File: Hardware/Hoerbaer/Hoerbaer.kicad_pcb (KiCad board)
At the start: 4 copper layers, 186 parts, among them J1 I2C, J10 LEDS, J11 LEDS, J12 Battery 1S Li-Ion, J13 JTAG, J14 Speaker_L, J15 Speaker_R, J16 USB2_UART, J2 DISPLAY, J3 Micro_SD_Card_Det1, J4 USB1, J5 ENCODER, J6 BUTTONS, J7 BUTTONS, J8 BUTTONS, J9 LEDS, Q1 DMG3415UQ-7, Q5 S8050, Q6 S8050, SW1 RESET, SW2 PROG, U1 ESP32 S3 MINI, U10 TAS5805M, U11 CH343P, U12 MAX17048G, U13 TPS61288, U2 PCF8574TS, U3 PCF8574TS, U4 PCF8574TS, U5 TLC59108xPW, U6 TLC59108xPW, U7 TLC59108xPW, U8 MCP73831T-2ACI/OT (4.2V), U9 TPS63001

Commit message: More numbers, changed HBI input package, i2c addresses, layout.
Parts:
- added C63: 100nF, Capacitor_SMD:C_0402_1005Metric, F.Cu at (52.5, -14.6)
- added D4: GREEN, LED_SMD:LED_0603_1608Metric, F.Cu at (155.4, -106.4)
- added H1: MountingHole_Pad, MountingHole:MountingHole_3.2mm_M3_Pad_Via, F.Cu at (31.3, 132.5)
- added H2: MountingHole_Pad, MountingHole:MountingHole_3.2mm_M3_Pad_Via, F.Cu at (31.3, 140.4)
- added H3: MountingHole_Pad, MountingHole:MountingHole_3.2mm_M3_Pad_Via, F.Cu at (31.3, 148.4)
- added H4: MountingHole_Pad, MountingHole:MountingHole_3.2mm_M3_Pad_Via, F.Cu at (31.3, 156.3)
- added J17: RST_BOOT, Connector_PinHeader_2.54mm:PinHeader_1x03_P2.54mm_Vertical, F.Cu at (146.7, -99.4)
- added R56: 5.1kΩ, Resistor_SMD:R_0402_1005Metric, F.Cu at (154.8, -104.1)
- J12, J14, J15: footprint Connector_Wire:SolderWire-0.75sqmm_1x02_P7mm_D1.25mm_OD3.5mm -> Connector_Phoenix_MSTB:PhoenixContact_MSTBVA_2,5_2-G-5,08_1x02_P5.08mm_Vertical
- J5: footprint Connector_PinHeader_2.54mm:PinHeader_1x03_P2.54mm_Vertical -> Connector_PinHeader_2.54mm:PinHeader_1x04_P2.54mm_Vertical
- U2, U3, U4: value PCF8574TS -> PCF8574APWR; footprint Package_SO:SOIC-16W_7.5x10.3mm_P1.27mm -> Package_SO:SSOP-20_4.4x6.5mm_P0.65mm
- moved D3 284.3 mm to (61.9, -85.7)
- moved C62 276.7 mm to (54.2, -86.0), turned to 180 degrees
- moved Q1 275.4 mm to (60.1, -89.6)
- moved C12 274.0 mm to (49.7, -70.8)
- moved C15 272.8 mm to (56.8, -74.2), turned to -90 degrees
- moved R62 269.9 mm to (65.3, -146.1)
- moved L1 269.8 mm to (50.2, -77.1)
- moved TP6 269.3 mm to (44.0, -71.0)
- moved R48 268.7 mm to (57.0, -90.6), turned to 180 degrees
- moved U9 266.0 mm to (50.2, -73.4), turned to -90 degrees
- moved R61 263.1 mm to (67.4, -140.7)
- moved R46 262.2 mm to (45.0, -71.0)
- moved R63 261.2 mm to (84.7, -149.4), turned to 180 degrees
- moved U8 261.2 mm to (72.7, -78.5)
- moved C13 261.1 mm to (47.1, -74.0), turned to -90 degrees
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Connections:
- net Net-(C21-Pad1) renamed /Power/12V_SW
- net Net-(D3-K) renamed /Power/SWITCHER_VIN
- net Net-(U9-L1) renamed /Power/3V3_L1
- net Net-(U9-L2) renamed /Power/3V3_L2
- U1 pad 17: unconnected-(U1-IO13-Pad17) -> Net-(U1-IO13)
- U2 pad 1: GND -> /HBI_INT
- U2 pad 10: Net-(J6-Pin_12) -> Net-(J6-Pin_2)
- U2 pad 11: Net-(J6-Pin_14) -> Net-(J6-Pin_4)
- U2 pad 12: Net-(J6-Pin_16) -> Net-(J6-Pin_6)
- U2 pad 13: /HBI_INT -> unconnected-(U2-NC-Pad13)
- U2 pad 14: /I2C1_SCL -> Net-(J6-Pin_8)
- U2 pad 15: /I2C1_SDA -> GND
- U2 pad 16: VCC -> Net-(J6-Pin_10)
- U2 pad 2: GND -> /I2C1_SCL
- U2 pad 3: GND -> unconnected-(U2-NC-Pad3)
- U2 pad 4: Net-(J6-Pin_2) -> /I2C1_SDA
- U2 pad 5: Net-(J6-Pin_4) -> VCC
- U2 pad 6: Net-(J6-Pin_6) -> GND
- U2 pad 7: Net-(J6-Pin_8) -> GND
- U2 pad 8: GND -> unconnected-(U2-NC-Pad8)
- U2 pad 9: Net-(J6-Pin_10) -> GND
- U3 pad 1: VCC -> /HBI_INT
- U3 pad 10: Net-(J7-Pin_12) -> Net-(J7-Pin_2)
- U3 pad 11: Net-(J7-Pin_14) -> Net-(J7-Pin_4)
- U3 pad 12: Net-(J7-Pin_16) -> Net-(J7-Pin_6)
- U3 pad 13: /HBI_INT -> unconnected-(U3-NC-Pad13)
- U3 pad 14: /I2C1_SCL -> Net-(J7-Pin_8)
- U3 pad 15: /I2C1_SDA -> GND
- U3 pad 16: VCC -> Net-(J7-Pin_10)
- U3 pad 2: GND -> /I2C1_SCL
- U3 pad 3: GND -> unconnected-(U3-NC-Pad3)
- U3 pad 4: Net-(J7-Pin_2) -> /I2C1_SDA
- U3 pad 5: Net-(J7-Pin_4) -> VCC
- U3 pad 6: Net-(J7-Pin_6) -> VCC
- U3 pad 7: Net-(J7-Pin_8) -> GND
- U3 pad 8: GND -> unconnected-(U3-NC-Pad8)
- U3 pad 9: Net-(J7-Pin_10) -> GND
- U4 pad 1: GND -> /HBI_INT
- U4 pad 10: Net-(J8-Pin_12) -> Net-(J8-Pin_2)
- U4 pad 11: Net-(J8-Pin_14) -> Net-(J8-Pin_4)
- U4 pad 12: Net-(J8-Pin_16) -> Net-(J8-Pin_6)
- U4 pad 13: /HBI_INT -> unconnected-(U4-NC-Pad13)
- U4 pad 14: /I2C1_SCL -> Net-(J8-Pin_8)
- U4 pad 15: /I2C1_SDA -> GND
- U4 pad 16: VCC -> Net-(J8-Pin_10)
- U4 pad 2: VCC -> /I2C1_SCL
- U4 pad 3: GND -> unconnected-(U4-NC-Pad3)
- U4 pad 4: Net-(J8-Pin_2) -> /I2C1_SDA
- U4 pad 5: Net-(J8-Pin_4) -> VCC
- U4 pad 6: Net-(J8-Pin_6) -> GND
- U4 pad 7: Net-(J8-Pin_8) -> VCC
- U4 pad 8: GND -> unconnected-(U4-NC-Pad8)
- U4 pad 9: Net-(J8-Pin_10) -> GND
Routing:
- net Net-(J16-CC1): track 0.00 -> 1.86 mm
- added copper zone on F.Cu, net +12V
- added copper zone on F.Cu, net /Power/12V_SW
- added copper zone on F.Cu, net /Power/3V3_L1
- added copper zone on F.Cu, net /Power/3V3_L2
- added copper zone on F.Cu, net /Power/SWITCHER_VIN
- added copper zone on F.Cu, net GNDPWR
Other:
- board outline added: 180 x 89 mm

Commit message: Layout drc error free
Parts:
- removed H4: MountingHole_Pad, MountingHole:MountingHole_3.2mm_M3_Pad_Via
- removed J10, J11: LEDS, Connector_PinHeader_2.54mm:PinHeader_2x08_P2.54mm_Vertical
- added C64: 100nF, Capacitor_SMD:C_0402_1005Metric, F.Cu at (117.2, 69.3)
- added C65: 10µF, Capacitor_SMD:C_0805_2012Metric, F.Cu at (66.2, 106.7)
- C56, C57: value 100nF -> 1uF
- C60: value 1nF -> 4.7nF
- C61: value 30pF -> 27pF
- J1: footprint Connector_PinHeader_2.54mm:PinHeader_1x03_P2.54mm_Vertical -> Connector_PinHeader_2.54mm:PinHeader_1x04_P2.54mm_Vertical
- J6: value BUTTONS -> PAW_A; footprint Connector_PinHeader_2.54mm:PinHeader_2x08_P2.54mm_Vertical -> Connector_PinHeader_2.54mm:PinHeader_2x12_P2.54mm_Vertical
- J7: value BUTTONS -> PAW_B; footprint Connector_PinHeader_2.54mm:PinHeader_2x08_P2.54mm_Vertical -> Connector_PinHeader_2.54mm:PinHeader_2x12_P2.54mm_Vertical
- J8: value BUTTONS -> PAW_C; footprint Connector_PinHeader_2.54mm:PinHeader_2x08_P2.54mm_Vertical -> Connector_PinHeader_2.54mm:PinHeader_2x12_P2.54mm_Vertical
- J9: value LEDS -> PAW_D; footprint Connector_PinHeader_2.54mm:PinHeader_2x08_P2.54mm_Vertical -> Connector_PinHeader_2.54mm:PinHeader_2x12_P2.54mm_Vertical
- R55: value 36.6kΩ -> 47kΩ
- TP1, TP10, TP2, TP3, TP4, TP5, TP6, TP7, TP8, TP9: moved to F.Cu
- moved J14 295.1 mm to (116.5, 142.5), turned to 180 degrees
- moved R63 287.9 mm to (115.0, 136.9), turned to 90 degrees
- moved C51 286.7 mm to (113.5, 137.4), turned to 0 degrees
- moved C46 285.8 mm to (113.5, 136.4), turned to 0 degrees
- moved R64 284.5 mm to (110.8, 136.9), turned to 90 degrees
- moved C52 283.3 mm to (109.3, 137.4), turned to 0 degrees
- moved FB2 282.4 mm to (112.3, 133.5), turned to -90 degrees
- moved C47 282.4 mm to (109.3, 136.4), turned to 0 degrees
- moved C54 281.5 mm to (104.9, 137.4), turned to 180 degrees
- moved J15 280.9 mm to (98.0, 143.5), turned to 0 degrees
- moved C45 280.4 mm to (114.8, 126.5), turned to 0 degrees
- moved FB3 279.5 mm to (108.8, 133.5), turned to -90 degrees
- moved R66 279.3 mm to (103.4, 136.9), turned to 90 degrees
- moved C43 279.2 mm to (112.0, 128.8), turned to 0 degrees
- moved C49 279.0 mm to (104.9, 136.4), turned to 180 degrees
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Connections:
- net Net-(J14-Pin_1) renamed /Audio/SPEAKER_A+
- net Net-(J14-Pin_2) renamed /Audio/SPEAKER_A-
- net Net-(J15-Pin_1) renamed /Audio/SPEAKER_B+
- net Net-(J15-Pin_2) renamed /Audio/SPEAKER_B-
- net Net-(U10-OUT_A+) renamed /Audio/AMP_OUT_A+
- net Net-(U10-OUT_A-) renamed /Audio/AMP_OUT_A-
- net Net-(U10-OUT_B+) renamed /Audio/AMP_OUT_B+
- net Net-(U10-OUT_B-) renamed /Audio/AMP_OUT_B-
- C25 pad 2: GNDPWR -> GND
- C56 pad 1: Net-(U11-VIO) -> VCC
- C57 pad 1: Net-(U11-VDD5) -> /USB_UART/USB2_VBUS
- J3 pad 11: unconnected-(J3-SHIELD-Pad11) -> GND
- J6 pad 1: Net-(J6-Pin_1) -> /HBI/PAW_A_B1
- J6 pad 10: Net-(J6-Pin_10) -> GND
- J6 pad 11: Net-(J6-Pin_1) -> /HBI/PAW_A_D3
- J6 pad 12: Net-(J6-Pin_12) -> +12V
- J6 pad 13: Net-(J6-Pin_1) -> /HBI/PAW_A_B4
- J6 pad 14: Net-(J6-Pin_14) -> GND
- J6 pad 15: GND -> /HBI/PAW_A_D4
- J6 pad 16: Net-(J6-Pin_16) -> +12V
- J6 pad 2: Net-(J6-Pin_2) -> GND
- J6 pad 3: Net-(J6-Pin_1) -> /HBI/PAW_A_D1
- J6 pad 4: Net-(J6-Pin_4) -> +12V
- J6 pad 5: Net-(J6-Pin_1) -> /HBI/PAW_A_B2
- J6 pad 6: Net-(J6-Pin_6) -> GND
- J6 pad 7: Net-(J6-Pin_1) -> /HBI/PAW_A_D2
- J6 pad 8: Net-(J6-Pin_8) -> +12V
- J6 pad 9: Net-(J6-Pin_1) -> /HBI/PAW_A_B3
- J7 pad 1: Net-(J7-Pin_1) -> /HBI/PAW_B_B1
- J7 pad 10: Net-(J7-Pin_10) -> GND
- J7 pad 11: Net-(J7-Pin_1) -> /HBI/PAW_B_D3
- J7 pad 12: Net-(J7-Pin_12) -> +12V
- J7 pad 13: Net-(J7-Pin_1) -> /HBI/PAW_B_B4
- J7 pad 14: Net-(J7-Pin_14) -> GND
- J7 pad 15: GND -> /HBI/PAW_B_D4
- J7 pad 16: Net-(J7-Pin_16) -> +12V
- J7 pad 2: Net-(J7-Pin_2) -> GND
- J7 pad 3: Net-(J7-Pin_1) -> /HBI/PAW_B_D1
- J7 pad 4: Net-(J7-Pin_4) -> +12V
- J7 pad 5: Net-(J7-Pin_1) -> /HBI/PAW_B_B2
- J7 pad 6: Net-(J7-Pin_6) -> GND
- J7 pad 7: Net-(J7-Pin_1) -> /HBI/PAW_B_D2
- J7 pad 8: Net-(J7-Pin_8) -> +12V
- J7 pad 9: Net-(J7-Pin_1) -> /HBI/PAW_B_B3
- J8 pad 1: Net-(J8-Pin_1) -> /HBI/PAW_C_B1
- J8 pad 10: Net-(J8-Pin_10) -> GND
- J8 pad 11: Net-(J8-Pin_1) -> /HBI/PAW_C_D3
- J8 pad 12: Net-(J8-Pin_12) -> +12V
- J8 pad 13: Net-(J8-Pin_1) -> /HBI/PAW_C_B4
- J8 pad 14: Net-(J8-Pin_14) -> GND
- J8 pad 15: GND -> /HBI/PAW_C_D4
- J8 pad 16: Net-(J8-Pin_16) -> +12V
- J8 pad 2: Net-(J8-Pin_2) -> GND
- J8 pad 3: Net-(J8-Pin_1) -> /HBI/PAW_C_D1
- J8 pad 4: Net-(J8-Pin_4) -> +12V
- J8 pad 5: Net-(J8-Pin_1) -> /HBI/PAW_C_B2
- J8 pad 6: Net-(J8-Pin_6) -> GND
- J8 pad 7: Net-(J8-Pin_1) -> /HBI/PAW_C_D2
- J8 pad 8: Net-(J8-Pin_8) -> +12V
- J8 pad 9: Net-(J8-Pin_1) -> /HBI/PAW_C_B3
- J9 pad 1: +12V -> /HBI/PAW_D_B1
- J9 pad 10: Net-(J9-Pin_10) -> GND
- J9 pad 11: +12V -> /HBI/PAW_D_D3
- J9 pad 12: Net-(J9-Pin_12) -> +12V
- J9 pad 13: +12V -> /HBI/PAW_D_B4
- J9 pad 14: Net-(J9-Pin_14) -> GND
- J9 pad 15: +12V -> /HBI/PAW_D_D4
- J9 pad 16: Net-(J9-Pin_16) -> +12V
- J9 pad 2: Net-(J9-Pin_2) -> GND
- J9 pad 3: +12V -> /HBI/PAW_D_D1
- J9 pad 4: Net-(J9-Pin_4) -> +12V
- J9 pad 5: +12V -> /HBI/PAW_D_B2
- J9 pad 6: Net-(J9-Pin_6) -> GND
- J9 pad 7: +12V -> /HBI/PAW_D_D2
- J9 pad 8: Net-(J9-Pin_8) -> +12V
- J9 pad 9: +12V -> /HBI/PAW_D_B3
- R19 pad 2: Net-(J6-Pin_2) -> /HBI/PAW_A_B1
- R20 pad 2: Net-(J7-Pin_2) -> /HBI/PAW_B_B3
- R21 pad 2: Net-(J8-Pin_2) -> /HBI/PAW_C_B5
- R22 pad 2: Net-(J6-Pin_4) -> /HBI/PAW_A_B2
- R23 pad 2: Net-(J7-Pin_4) -> /HBI/PAW_B_B4
- R24 pad 2: Net-(J8-Pin_4) -> /HBI/PAW_C_B6
- R25 pad 2: Net-(J6-Pin_6) -> /HBI/PAW_A_B3
- R26 pad 2: Net-(J7-Pin_6) -> /HBI/PAW_B_B5
- R27 pad 2: Net-(J8-Pin_6) -> /HBI/PAW_D_B1
- R28 pad 2: Net-(J6-Pin_8) -> /HBI/PAW_A_B4
- R29 pad 2: Net-(J7-Pin_8) -> /HBI/PAW_B_B6
- R30 pad 2: Net-(J8-Pin_8) -> /HBI/PAW_D_B2
- R31 pad 2: Net-(J6-Pin_10) -> /HBI/PAW_A_B5
- R32 pad 2: Net-(J7-Pin_10) -> /HBI/PAW_C_B1
- R33 pad 2: Net-(J8-Pin_10) -> /HBI/PAW_D_B3
- R34 pad 2: Net-(J6-Pin_12) -> /HBI/PAW_A_B6
- R35 pad 2: Net-(J7-Pin_12) -> /HBI/PAW_C_B2
- R36 pad 2: Net-(J8-Pin_12) -> /HBI/PAW_D_B4
- R37 pad 2: Net-(J6-Pin_14) -> /HBI/PAW_B_B1
- R38 pad 2: Net-(J7-Pin_14) -> /HBI/PAW_C_B3
- R39 pad 2: Net-(J8-Pin_14) -> /HBI/PAW_D_B5
- R40 pad 2: Net-(J6-Pin_16) -> /HBI/PAW_B_B2
- R41 pad 2: Net-(J7-Pin_16) -> /HBI/PAW_C_B4
- R42 pad 2: Net-(J8-Pin_16) -> /HBI/PAW_D_B6
- U11 pad 1: Net-(U11-VIO) -> VCC
- U11 pad 3: Net-(U11-VDD5) -> /USB_UART/USB2_VBUS
- U2 pad 10: Net-(J6-Pin_2) -> /HBI/PAW_A_B1
- U2 pad 11: Net-(J6-Pin_4) -> /HBI/PAW_A_B2
- U2 pad 12: Net-(J6-Pin_6) -> /HBI/PAW_A_B3
- U2 pad 14: Net-(J6-Pin_8) -> /HBI/PAW_A_B4
- U2 pad 16: Net-(J6-Pin_10) -> /HBI/PAW_A_B5
- U2 pad 17: Net-(J6-Pin_12) -> /HBI/PAW_A_B6
- U2 pad 19: Net-(J6-Pin_14) -> /HBI/PAW_B_B1
- U2 pad 20: Net-(J6-Pin_16) -> /HBI/PAW_B_B2
- U3 pad 10: Net-(J7-Pin_2) -> /HBI/PAW_B_B3
- U3 pad 11: Net-(J7-Pin_4) -> /HBI/PAW_B_B4
- U3 pad 12: Net-(J7-Pin_6) -> /HBI/PAW_B_B5
- U3 pad 14: Net-(J7-Pin_8) -> /HBI/PAW_B_B6
- U3 pad 16: Net-(J7-Pin_10) -> /HBI/PAW_C_B1
- U3 pad 17: Net-(J7-Pin_12) -> /HBI/PAW_C_B2
- U3 pad 19: Net-(J7-Pin_14) -> /HBI/PAW_C_B3
- U3 pad 20: Net-(J7-Pin_16) -> /HBI/PAW_C_B4
- U4 pad 10: Net-(J8-Pin_2) -> /HBI/PAW_C_B5
- U4 pad 11: Net-(J8-Pin_4) -> /HBI/PAW_C_B6
- U4 pad 12: Net-(J8-Pin_6) -> /HBI/PAW_D_B1
- U4 pad 14: Net-(J8-Pin_8) -> /HBI/PAW_D_B2
- U4 pad 16: Net-(J8-Pin_10) -> /HBI/PAW_D_B3
- U4 pad 17: Net-(J8-Pin_12) -> /HBI/PAW_D_B4
- U4 pad 19: Net-(J8-Pin_14) -> /HBI/PAW_D_B5
- U4 pad 20: Net-(J8-Pin_16) -> /HBI/PAW_D_B6
- U5 pad 10: Net-(J9-Pin_8) -> /HBI/PAW_A_D4
- U5 pad 11: Net-(J9-Pin_10) -> /HBI/PAW_A_D5
- U5 pad 12: Net-(J9-Pin_12) -> /HBI/PAW_A_D6
- U5 pad 14: Net-(J9-Pin_14) -> /HBI/PAW_B_D1
- U5 pad 15: Net-(J9-Pin_16) -> /HBI/PAW_B_D2
- U5 pad 6: Net-(J9-Pin_2) -> /HBI/PAW_A_D1
- U5 pad 7: Net-(J9-Pin_4) -> /HBI/PAW_A_D2
- U5 pad 9: Net-(J9-Pin_6) -> /HBI/PAW_A_D3
- U6 pad 10: Net-(J10-Pin_8) -> /HBI/PAW_B_D6
- U6 pad 11: Net-(J10-Pin_10) -> /HBI/PAW_C_D1
- U6 pad 12: Net-(J10-Pin_12) -> /HBI/PAW_C_D2
- U6 pad 14: Net-(J10-Pin_14) -> /HBI/PAW_C_D3
- U6 pad 15: Net-(J10-Pin_16) -> /HBI/PAW_C_D4
- U6 pad 6: Net-(J10-Pin_2) -> /HBI/PAW_B_D3
- U6 pad 7: Net-(J10-Pin_4) -> /HBI/PAW_B_D4
- U6 pad 9: Net-(J10-Pin_6) -> /HBI/PAW_B_D5
- U7 pad 10: Net-(J11-Pin_8) -> /HBI/PAW_D_D2
- U7 pad 11: Net-(J11-Pin_10) -> /HBI/PAW_D_D3
- U7 pad 12: Net-(J11-Pin_12) -> /HBI/PAW_D_D4
- U7 pad 14: Net-(J11-Pin_14) -> /HBI/PAW_D_D5
- U7 pad 15: Net-(J11-Pin_16) -> /HBI/PAW_D_D6
- U7 pad 6: Net-(J11-Pin_2) -> /HBI/PAW_C_D5
- U7 pad 7: Net-(J11-Pin_4) -> /HBI/PAW_C_D6
- U7 pad 9: Net-(J11-Pin_6) -> /HBI/PAW_D_D1
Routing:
- net /I2C1_SCL: track 0.00 -> 203.1 mm, vias 0 -> 10
- net /I2C1_SDA: track 0.00 -> 201.6 mm, vias 0 -> 9
- net GND: track 0.00 -> 165.5 mm, vias 0 -> 176
- net /HBI_INT: track 0.00 -> 116.5 mm, vias 0 -> 5
- net /HBI_RST: track 0.00 -> 111.5 mm, vias 0 -> 6
- net +12V: track 0.00 -> 95.6 mm, vias 0 -> 28
- net /MCU_~{RST}: track 0.00 -> 85.8 mm, vias 0 -> 6
- net /MCU_IO0: track 0.00 -> 80.2 mm, vias 0 -> 2
- net VCC: track 0.00 -> 80.2 mm, vias 0 -> 58
- net /CODEC_~{PDN}: track 0.00 -> 73.6 mm, vias 0 -> 2
- net /I2S1_DOUT: track 0.00 -> 69.5 mm, vias 0 -> 2
- net /I2S1_BCLK: track 0.00 -> 69.1 mm, vias 0 -> 2
- net /I2S1_WS: track 0.00 -> 69.0 mm, vias 0 -> 2
- net /MCU_TXD: track 0.00 -> 63.7 mm, vias 0 -> 2
- net /MCU_RXD: track 0.00 -> 62.8 mm, vias 0 -> 2
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- added copper zone on In1.Cu, net +12V
- added copper zone on F.Cu, net +BATT
- added copper zone on F.Cu, net /Audio/AMP_OUT_A+
- added copper zone on F.Cu, net /Audio/AMP_OUT_A-
- added copper zone on F.Cu, net /Audio/AMP_OUT_B+
- added copper zone on F.Cu, net /Audio/AMP_OUT_B-
- added copper zone on F.Cu, net /Audio/PVDD
- added copper zone on In1.Cu, net /Audio/PVDD
- added copper zone on F.Cu, net /Audio/SPEAKER_A+
- added copper zone on F.Cu, net /Audio/SPEAKER_A-
- added copper zone on F.Cu, net /Audio/SPEAKER_B+
- added copper zone on F.Cu, net /Audio/SPEAKER_B-
- added copper zone on B.Cu, net GND
- added copper zone on F.Cu, net GND
- added copper zone on In2.Cu, net GND
- added copper zone on F.Cu, net VBUS
- added copper zone on F.Cu, net VCC
- added copper zone on In1.Cu, net VCC
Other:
- board size 180 x 89 mm -> 80 x 88 mm

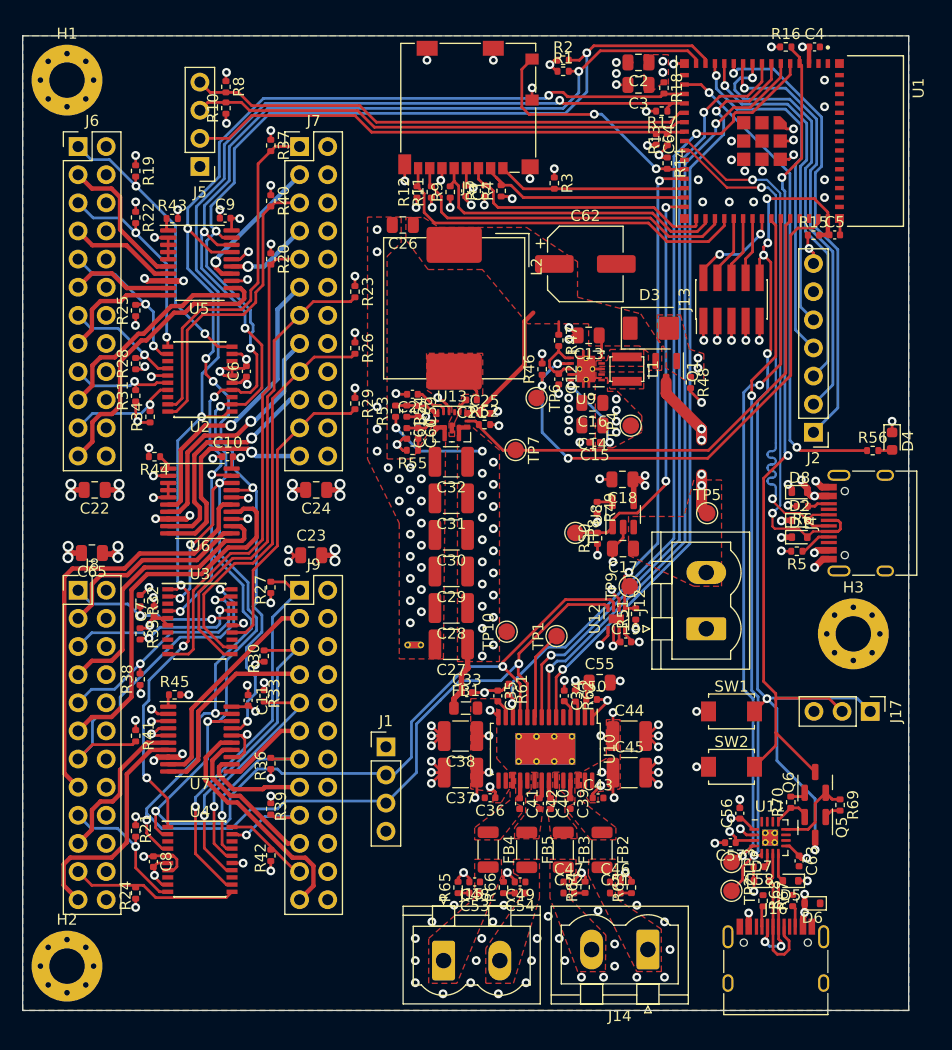
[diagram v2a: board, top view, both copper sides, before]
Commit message: Adjos refdes silkscreen
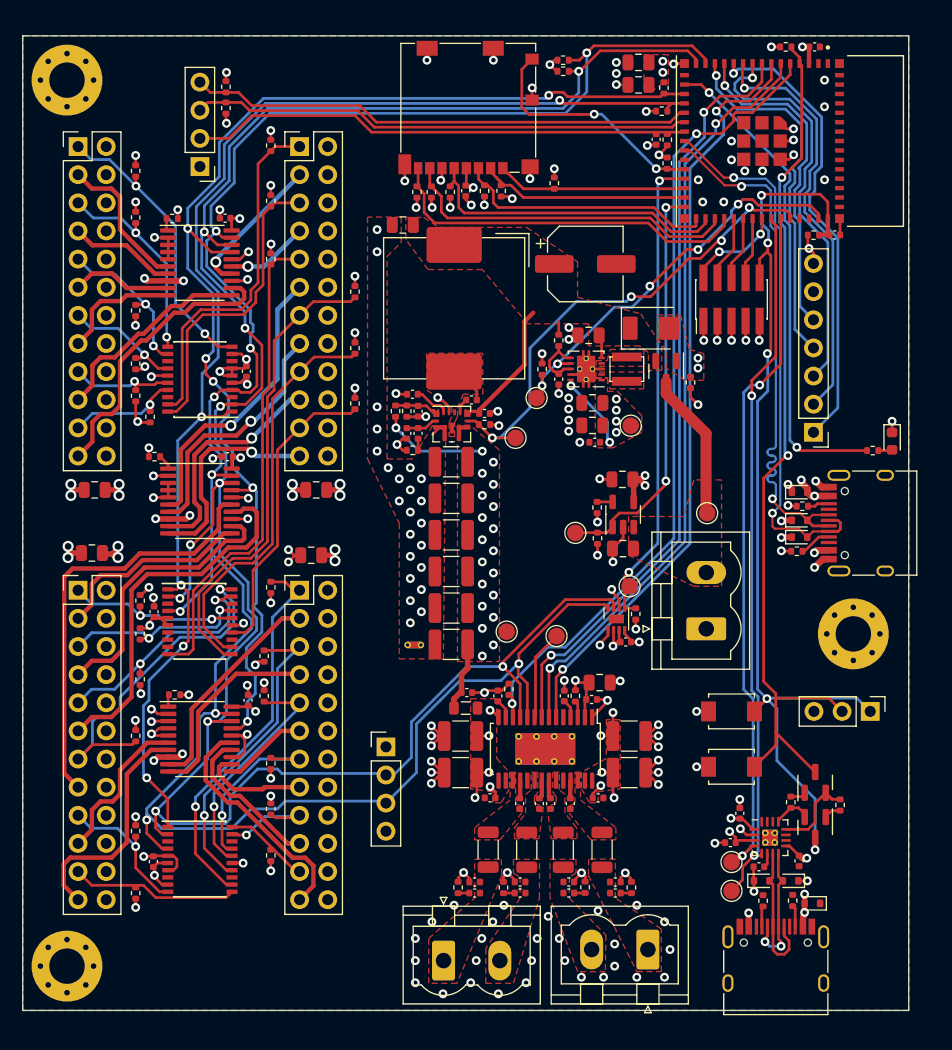
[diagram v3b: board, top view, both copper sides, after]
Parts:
- moved TP7 1.10 mm to (104.5, 96.3)
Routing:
- net /3V3_~{PSAVE}: track 52.8 -> 37.2 mm, vias 3 -> 5
- net /12V_EN: track 46.9 -> 44.6 mm, vias 0 -> 4
- net /MCU_~{RST}: track 85.8 -> 87.8 mm, vias 6 -> 5
- net VBUS: track 46.5 -> 45.6 mm
- net /SPI2_CLK: track 32.4 -> 33.1 mm
- net /SPI2_MOSI: track 29.4 -> 29.9 mm
- net GND: vias 176 -> 174
- net +BATT: vias 5 -> 1

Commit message: Drachosaurus added
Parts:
- removed TP1: SDOUT, TestPoint:TestPoint_Pad_D1.5mm
- added G***: LOGO, LOGO, F.Cu at (86.4, 64.5)
- added G***: LOGO, LOGO, F.Cu at (70.2, 64.5)
- added G***: LOGO, LOGO, F.Cu at (86.4, 143.5)
- added G***: LOGO, LOGO, F.Cu at (70.2, 143.5)
- added G***: LOGO, LOGO, B.Cu at (118.1, 91.5)
- added REF**: OSHW-Logo_11.4x12mm_SilkScreen, Symbol:OSHW-Logo_11.4x12mm_SilkScreen, B.Cu at (76.5, 141.0)
- TP2: value TestPoint -> MCU_TX
- TP3: value TestPoint -> MCU_RX
- moved TP9 2.97 mm to (112.0, 108.7), turned to 180 degrees
- moved J17 0.40 mm to (136.5, 120.6)
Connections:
- U10 pad 9: Net-(U10-SDOUT) -> unconnected-(U10-SDOUT-Pad9)
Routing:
- net Net-(U10-SDOUT): track 8.15 -> 0.00 mm
- net /BAT_~{ALERT}: track 43.2 -> 45.7 mm
- net +12V: track 95.6 -> 97.3 mm
- net /12V_EN: track 44.6 -> 43.0 mm
- net /I2C1_SCL: track 203.1 -> 204.1 mm
- net /I2C1_SDA: track 201.6 -> 200.8 mm
- net GND: track 165.5 -> 166.4 mm, vias 174 -> 175
- net /MCU_IO0: track 80.3 -> 81.1 mm
- net /MCU_~{RST}: track 87.8 -> 88.5 mm
- net /CODEC_~{PDN}: track 73.6 -> 73.0 mm
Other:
- board text added: "A"
- board text added: "B"
- board text added: "B1"
- board text added: "B2"
- board text added: "B3"
- board text added: "B4"
- board text added: "B5"
- board text added: "B6"
- board text added: "BOOT"
- board text added: "BTN"
- board text added: "C"
- board text added: "CLK"
- board text added: "CS"
- board text added: "D"
- board text added: "D1"
- board text added: "D2"
- board text added: "D3"
- board text added: "D4"
- board text added: "D5"
- board text added: "D6"
- board text added: "DC"
- board text added: "Encoder"
- board text added: "GND"
- board text added: "I^{2}C"
- board text added: "MOSI"
- board text added: "RST"
- board text added: "SCL"
- board text added: "SDA"
- board text added: "USB UART"
- board text added: "VCC"
